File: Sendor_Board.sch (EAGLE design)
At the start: 19 parts, among them Q1 8.000Mhz, U1 PIC32MX795F512H-80I/PT, X1 MINI-USB-SHIELD-UX60A-MB-5ST

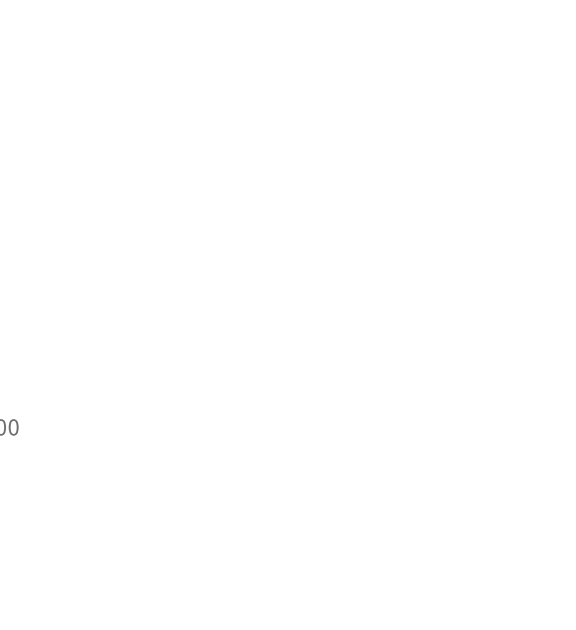
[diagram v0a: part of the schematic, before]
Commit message: Add SHT25 to shema
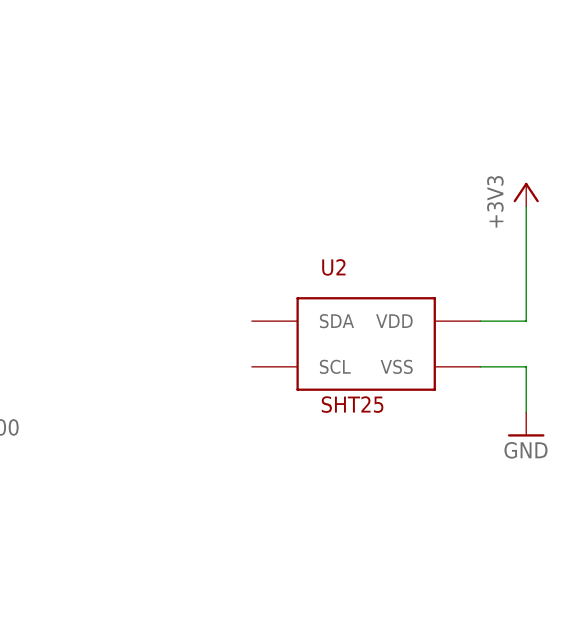
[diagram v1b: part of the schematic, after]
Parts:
- added U2: SHT25, pfo:SHT25
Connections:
- net +3V3: now also U2.VDD
- net GND: now also U2.VSS
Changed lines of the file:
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@@
 <grid distance="0.1" unitdist="inch" unit="inch" style="lines" multiple="1" display="no" altdistance="0.01" altunitdist="inch" altunit="inch"/>
 <layers>
-<layer number="1" name="Top" color="4" fill="1" visible="no" active="no"/>
-<layer number="16" name="Bottom" color="1" fill="1" visible="no" active="no"/>
-<layer number="17" name="Pads" color="2" fill="1" visible="no" active="no"/>
-<layer number="18" name="Vias" color="2" fill="1" visible="no" active="no"/>
-<layer number="19" name="Unrouted" color="6" fill="1" visible="no" active="no"/>
-<layer number="20" name="Dimension" color="15" fill="1" visible="no" active="no"/>
-<layer number="21" name="tPlace" color="7" fill="1" visible="no" active="no"/>
-<layer number="22" name="bPlace" color="7" fill="1" visible="no" active="no"/>
-<layer number="23" name="tOrigins" color="15" fill="1" visible="no" active="no"/>
-<layer number="24" name="bOrigins" color="15" fill="1" visible="no" active="no"/>
-<layer number="25" name="tNames" color="7" fill="1" visible="no" active="no"/>
-<layer number="26" name="bNames" color="7" fill="1" visible="no" active="no"/>
-<layer number="27" name="tValues" color="7" fill="1" visible="no" active="no"/>
-<layer number="28" name="bValues" color="7" fill="1" visible="no" active="no"/>
+<layer number="1" name="Top" color="4" fill="1" visible="yes" active="no"/>
+<layer number="16" name="Bottom" color="1" fill="1" visible="yes" active="no"/>
+<layer number="17" name="Pads" color="2" fill="1" visible="yes" active="no"/>
+<layer number="18" name="Vias" color="2" fill="1" visible="yes" active="no"/>
+<layer number="19" name="Unrouted" color="6" fill="1" visible="yes" active="no"/>
+<layer number="20" name="Dimension" color="15" fill="1" visible="yes" active="no"/>
+<layer number="21" name="tPlace" color="7" fill="1" visible="yes" active="no"/>
+<layer number="22" name="bPlace" color="7" fill="1" visible="yes" active="no"/>
+<layer number="23" name="tOrigins" color="15" fill="1" visible="yes" active="no"/>
+<layer number="24" name="bOrigins" color="15" fill="1" visible="yes" active="no"/>
+<layer number="25" name="tNames" color="7" fill="1" visible="yes" active="no"/>
+<layer number="26" name="bNames" color="7" fill="1" visible="yes" active="no"/>
+<layer number="27" name="tValues" color="7" fill="1" visible="yes" active="no"/>
+<layer number="28" name="bValues" color="7" fill="1" visible="yes" active="no"/>
 <layer number="29" name="tStop" color="7" fill="3" visible="no" active="no"/>
 <layer number="30" name="bStop" color="7" fill="6" visible="no" active="no"/>
@@
 <layer number="35" name="tGlue" color="7" fill="4" visible="no" active="no"/>
 <layer number="36" name="bGlue" color="7" fill="5" visible="no" active="no"/>
-<layer number="37" name="tTest" color="7" fill="1" visible="no" active="no"/>
-<layer number="38" name="bTest" color="7" fill="1" visible="no" active="no"/>
+<layer number="37" name="tTest" color="7" fill="1" visible="yes" active="no"/>
+<layer number="38" name="bTest" color="7" fill="1" visible="yes" active="no"/>
 <layer number="39" name="tKeepout" color="4" fill="11" visible="no" active="no"/>
 <layer number="40" name="bKeepout" color="1" fill="11" visible="no" active="no"/>
@@
 <layer number="44" name="Drills" color="7" fill="1" visible="no" active="no"/>
 <layer number="45" name="Holes" color="7" fill="1" visible="no" active="no"/>
-<layer number="46" name="Milling" color="3" fill="1" visible="no" active="no"/>
-<layer number="47" name="Measures" color="7" fill="1" visible="no" active="no"/>
-<layer number="48" name="Document" color="7" fill="1" visible="no" active="no"/>
-<layer number="49" name="Reference" color="7" fill="1" visible="no" active="no"/>
-<layer number="51" name="tDocu" color="7" fill="1" visible="no" active="no"/>
-<layer number="52" name="bDocu" color="7" fill="1" visible="no" active="no"/>
+<layer number="46" name="Milling" color="3" fill="1" visible="yes" active="no"/>
+<layer number="47" name="Measures" color="7" fill="1" visible="yes" active="no"/>
+<layer number="48" name="Document" color="7" fill="1" visible="yes" active="no"/>
+<layer number="49" name="Reference" color="7" fill="1" visible="yes" active="no"/>
+<layer number="51" name="tDocu" color="7" fill="1" visible="yes" active="no"/>
+<layer number="52" name="bDocu" color="7" fill="1" visible="yes" active="no"/>
 <layer number="90" name="Modules" color="5" fill="1" visible="yes" active="yes"/>
 <layer number="91" name="Nets" color="2" fill="1" visible="yes" active="yes"/>
@@
 <part name="GND7" library="supply1" deviceset="GND" device=""/>
 <part name="X1" library="con-hirose" deviceset="MINI-USB-SHIELD-" device="UX60A-MB-5ST"/>
+<part name="U2" library="pfo" deviceset="SHT25" device=""/>
+<part name="GND8" library="supply1" deviceset="GND" device=""/>
+<part name="+3V2" library="supply1" deviceset="+3V3" device=""/>
 </parts>
 <sheets>
@@
 <instance part="GND7" gate="1" x="208.28" y="0"/>
 <instance part="X1" gate="G$1" x="215.9" y="-40.64"/>
+<instance part="U2" gate="G$1" x="233.68" y="68.58"/>
+<instance part="GND8" gate="1" x="251.46" y="58.42"/>
+<instance part="+3V2" gate="G$1" x="251.46" y="86.36"/>
 </instances>
 <busses>
@@
 <junction x="208.28" y="12.7"/>
 </segment>
+<segment>
+<pinref part="U2" gate="G$1" pin="VSS"/>
+<pinref part="GND8" gate="1" pin="GND"/>
+<wire x1="246.38" y1="66.04" x2="251.46" y2="66.04" width="0.1524" layer="91"/>
+<wire x1="251.46" y1="66.04" x2="251.46" y2="60.96" width="0.1524" layer="91"/>
+</segment>
 </net>
 <net name="+3V3" class="0">
@@
 <junction x="-96.52" y="101.6"/>
 </segment>
+<segment>
+<pinref part="U2" gate="G$1" pin="VDD"/>
+<pinref part="+3V2" gate="G$1" pin="+3V3"/>
+<wire x1="246.38" y1="71.12" x2="251.46" y2="71.12" width="0.1524" layer="91"/>
+<wire x1="251.46" y1="71.12" x2="251.46" y2="83.82" width="0.1524" layer="91"/>
+</segment>
 </net>

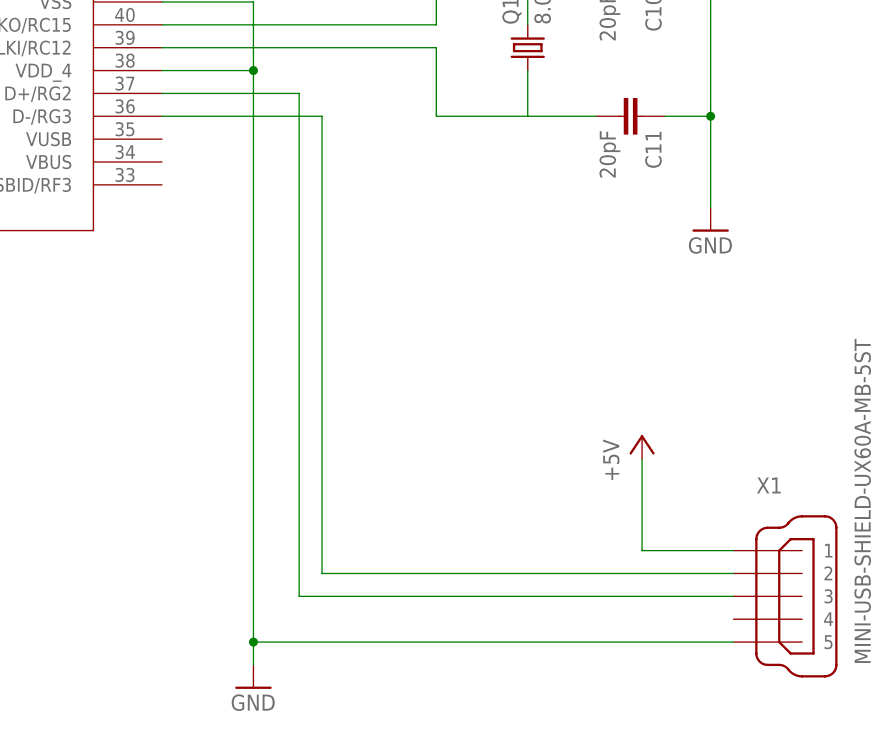
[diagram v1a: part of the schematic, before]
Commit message: Add net USBID
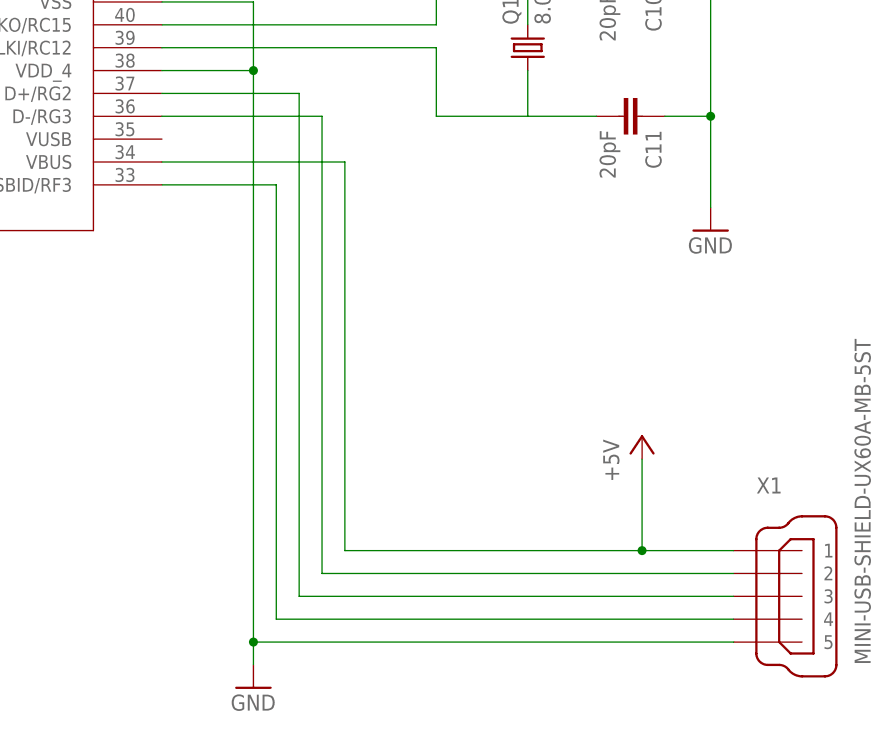
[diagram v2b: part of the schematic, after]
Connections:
- new net N$8: U1.USBID/RF3, X1G$1.4
- net +5V: now also U1.VBUS

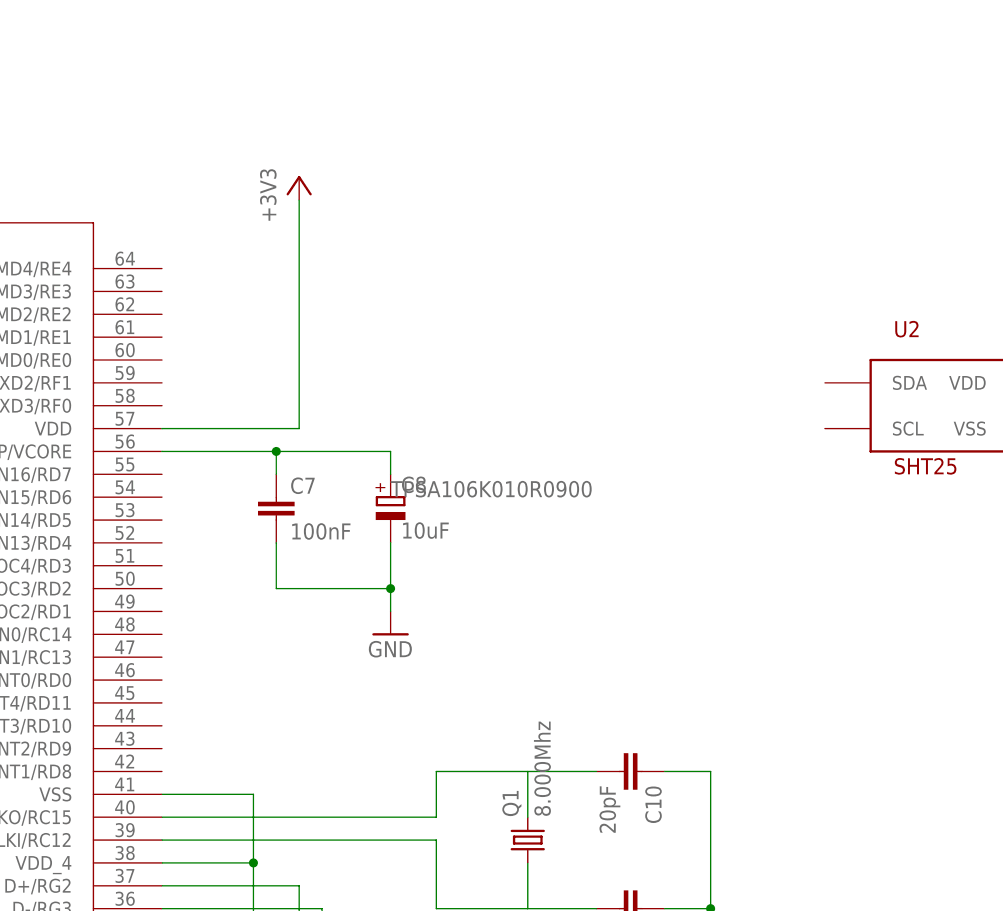
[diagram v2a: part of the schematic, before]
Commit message: Add I2C bus for SHT25
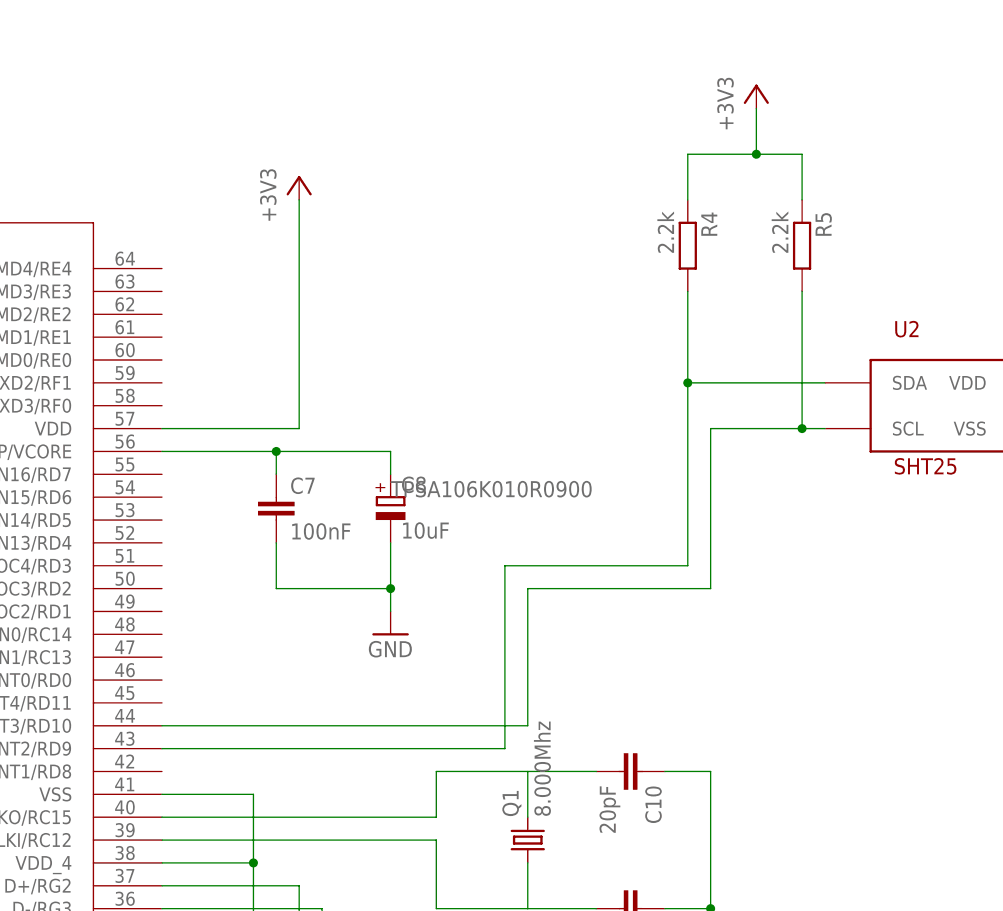
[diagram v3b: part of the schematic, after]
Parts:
- added R4, R5: 2.2k, resistor:R-EU_R1206
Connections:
- new net N$11: R4.2, U1.AERXD0/ETXD2/*SS1A/U1BRX/*U1ACTS/SDA1/IC2/INT2/RD9, U2.SDA
- new net N$12: R5.2, U1.ECOL/AERXDV/SCL1/IC3/PMCS2/PMA15/INT3/RD10, U2.SCL
- net +3V3: now also R4.1, R5.1
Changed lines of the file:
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@@
 <part name="+3V2" library="supply1" deviceset="+3V3" device=""/>
 <part name="U1" library="pfo" deviceset="PIC32MX795F512H-80I/PT" device=""/>
+<part name="R4" library="resistor" deviceset="R-EU_" device="R1206" value="2.2k"/>
+<part name="R5" library="resistor" deviceset="R-EU_" device="R1206" value="2.2k"/>
+<part name="+3V3" library="supply1" deviceset="+3V3" device=""/>
 </parts>
 <sheets>
@@
 <instance part="+3V2" gate="G$1" x="251.46" y="86.36"/>
 <instance part="U1" gate="A" x="0" y="83.82"/>
+<instance part="R4" gate="G$1" x="205.74" y="86.36" rot="R270"/>
+<instance part="R5" gate="G$1" x="218.44" y="86.36" rot="R270"/>
+<instance part="+3V3" gate="G$1" x="213.36" y="104.14"/>
 </instances>
 <busses>
@@
 <wire x1="251.46" y1="71.12" x2="251.46" y2="83.82" width="0.1524" layer="91"/>
 </segment>
+<segment>
+<pinref part="R4" gate="G$1" pin="1"/>
+<wire x1="205.74" y1="91.44" x2="205.74" y2="96.52" width="0.1524" layer="91"/>
+<pinref part="R5" gate="G$1" pin="1"/>
+<wire x1="205.74" y1="96.52" x2="213.36" y2="96.52" width="0.1524" layer="91"/>
+<wire x1="213.36" y1="96.52" x2="218.44" y2="96.52" width="0.1524" layer="91"/>
+<wire x1="218.44" y1="96.52" x2="218.44" y2="91.44" width="0.1524" layer="91"/>
+<pinref part="+3V3" gate="G$1" pin="+3V3"/>
+<wire x1="213.36" y1="101.6" x2="213.36" y2="96.52" width="0.1524" layer="91"/>
+<junction x="213.36" y="96.52"/>
+</segment>
 </net>
 <net name="N$1" class="0">
@@
 </segment>
 </net>
+<net name="N$11" class="0">
+<segment>
+<pinref part="U1" gate="A" pin="AERXD0/ETXD2/*SS1A/U1BRX/*U1ACTS/SDA1/IC2/INT2/RD9"/>
+<wire x1="147.32" y1="30.48" x2="185.42" y2="30.48" width="0.1524" layer="91"/>
+<wire x1="185.42" y1="30.48" x2="185.42" y2="50.8" width="0.1524" layer="91"/>
+<wire x1="185.42" y1="50.8" x2="205.74" y2="50.8" width="0.1524" layer="91"/>
+<wire x1="205.74" y1="50.8" x2="205.74" y2="71.12" width="0.1524" layer="91"/>
+<pinref part="U2" gate="G$1" pin="SDA"/>
+<wire x1="220.98" y1="71.12" x2="205.74" y2="71.12" width="0.1524" layer="91"/>
+<wire x1="205.74" y1="71.12" x2="205.74" y2="81.28" width="0.1524" layer="91"/>
+<junction x="205.74" y="71.12"/>
+<pinref part="R4" gate="G$1" pin="2"/>
+</segment>
+</net>
+<net name="N$12" class="0">
+<segment>
+<pinref part="U1" gate="A" pin="ECOL/AERXDV/SCL1/IC3/PMCS2/PMA15/INT3/RD10"/>
+<wire x1="147.32" y1="33.02" x2="187.96" y2="33.02" width="0.1524" layer="91"/>
+<wire x1="187.96" y1="33.02" x2="187.96" y2="48.26" width="0.1524" layer="91"/>
+<wire x1="187.96" y1="48.26" x2="208.28" y2="48.26" width="0.1524" layer="91"/>
+<wire x1="208.28" y1="48.26" x2="208.28" y2="66.04" width="0.1524" layer="91"/>
+<pinref part="U2" gate="G$1" pin="SCL"/>
+<wire x1="208.28" y1="66.04" x2="218.44" y2="66.04" width="0.1524" layer="91"/>
+<wire x1="220.98" y1="66.04" x2="218.44" y2="66.04" width="0.1524" layer="91"/>
+<wire x1="218.44" y1="66.04" x2="218.44" y2="81.28" width="0.1524" layer="91"/>
+<junction x="218.44" y="66.04"/>
+<pinref part="R5" gate="G$1" pin="2"/>
+</segment>
+</net>
